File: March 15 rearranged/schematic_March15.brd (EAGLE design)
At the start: 200.3 x 216.6 mm, 315 parts, among them CON1 UBC05V128-B0C04D, IC1 FT232RL, IC10 TL084D, IC13 7805TV, IC3 TL084D, IC4 TL084D, IC5 TL084D, IC6 TL084D, IC7 TL084D, IC8 TL084D, IC9 TL084D, Q2 BC557, T1 BC547, T2 BC547, U1 TMS320F28069_PN_80, U10 REF2030AIDDCR, U2 TLV5610_PW_20, U3 REF2030AIDDCR, U4 REF2030AIDDCR, U5 TS12A44514DR, U6 TS12A44514DR, U7 TPS7333QD, U8 REF2030AIDDCR, U9 MAX395CWG+

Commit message: Rearranged analog part to make the board smaller
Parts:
- moved R66 22.8 mm to (110.4, 25.3), flipped to the bottom
- moved R67 22.7 mm to (110.3, 29.2), flipped to the bottom
- moved JP42 20.4 mm to (145.3, 17.2), turned to 270 degrees
- moved JP43 18.7 mm to (143.4, -12.3), turned to 90 degrees
- moved JP13 17.6 mm to (139.5, 17.1), turned to 270 degrees
- moved JP68 16.9 mm to (121.4, 35.6)
- moved JP16 16.8 mm to (137.5, -12.4), turned to 270 degrees
- moved R64 16.5 mm to (116.0, 20.8), flipped to the bottom, turned to 180 degrees
- moved D14 15.3 mm to (117.1, 16.5)
- moved R127 14.9 mm to (113.6, 16.7)
- moved D15 13.4 mm to (109.8, 16.5), turned to 90 degrees
- moved C66 12.1 mm to (115.7, 30.9), flipped to the bottom, turned to 0 degrees
- moved R49 11.3 mm to (109.0, 34.0)
- moved C27 11.3 mm to (104.1, 19.2)
- moved C75 11.3 mm to (102.9, 27.9)
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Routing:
- net +5V: track 1057.4 -> 964.1 mm, vias 18 -> 15
- net ADCINA5: track 93.9 -> 140.8 mm
- net INTINP6: track 34.9 -> 72.9 mm, vias 1 -> 3
- net -5V: track 665.3 -> 640.2 mm, vias 12 -> 11
- net INTSWITCH4: track 10.9 -> 35.1 mm, vias 1 -> 0
- net INTINP4: track 53.4 -> 74.8 mm, vias 0 -> 1
- net INT_CONTROL: track 134.8 -> 113.7 mm
- net +3V3: track 515.0 -> 494.5 mm, vias 20 -> 19
- net DACO7: track 109.2 -> 129.1 mm
- net DACO5: track 97.7 -> 114.2 mm, vias 2 -> 3
- net OUT3: track 8.50 -> 22.0 mm, vias 0 -> 1
- net X8: track 73.6 -> 86.8 mm
- net INTSWITCH8: track 66.8 -> 79.6 mm
- net X4: track 28.0 -> 39.8 mm
- net X6: track 31.8 -> 43.6 mm
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
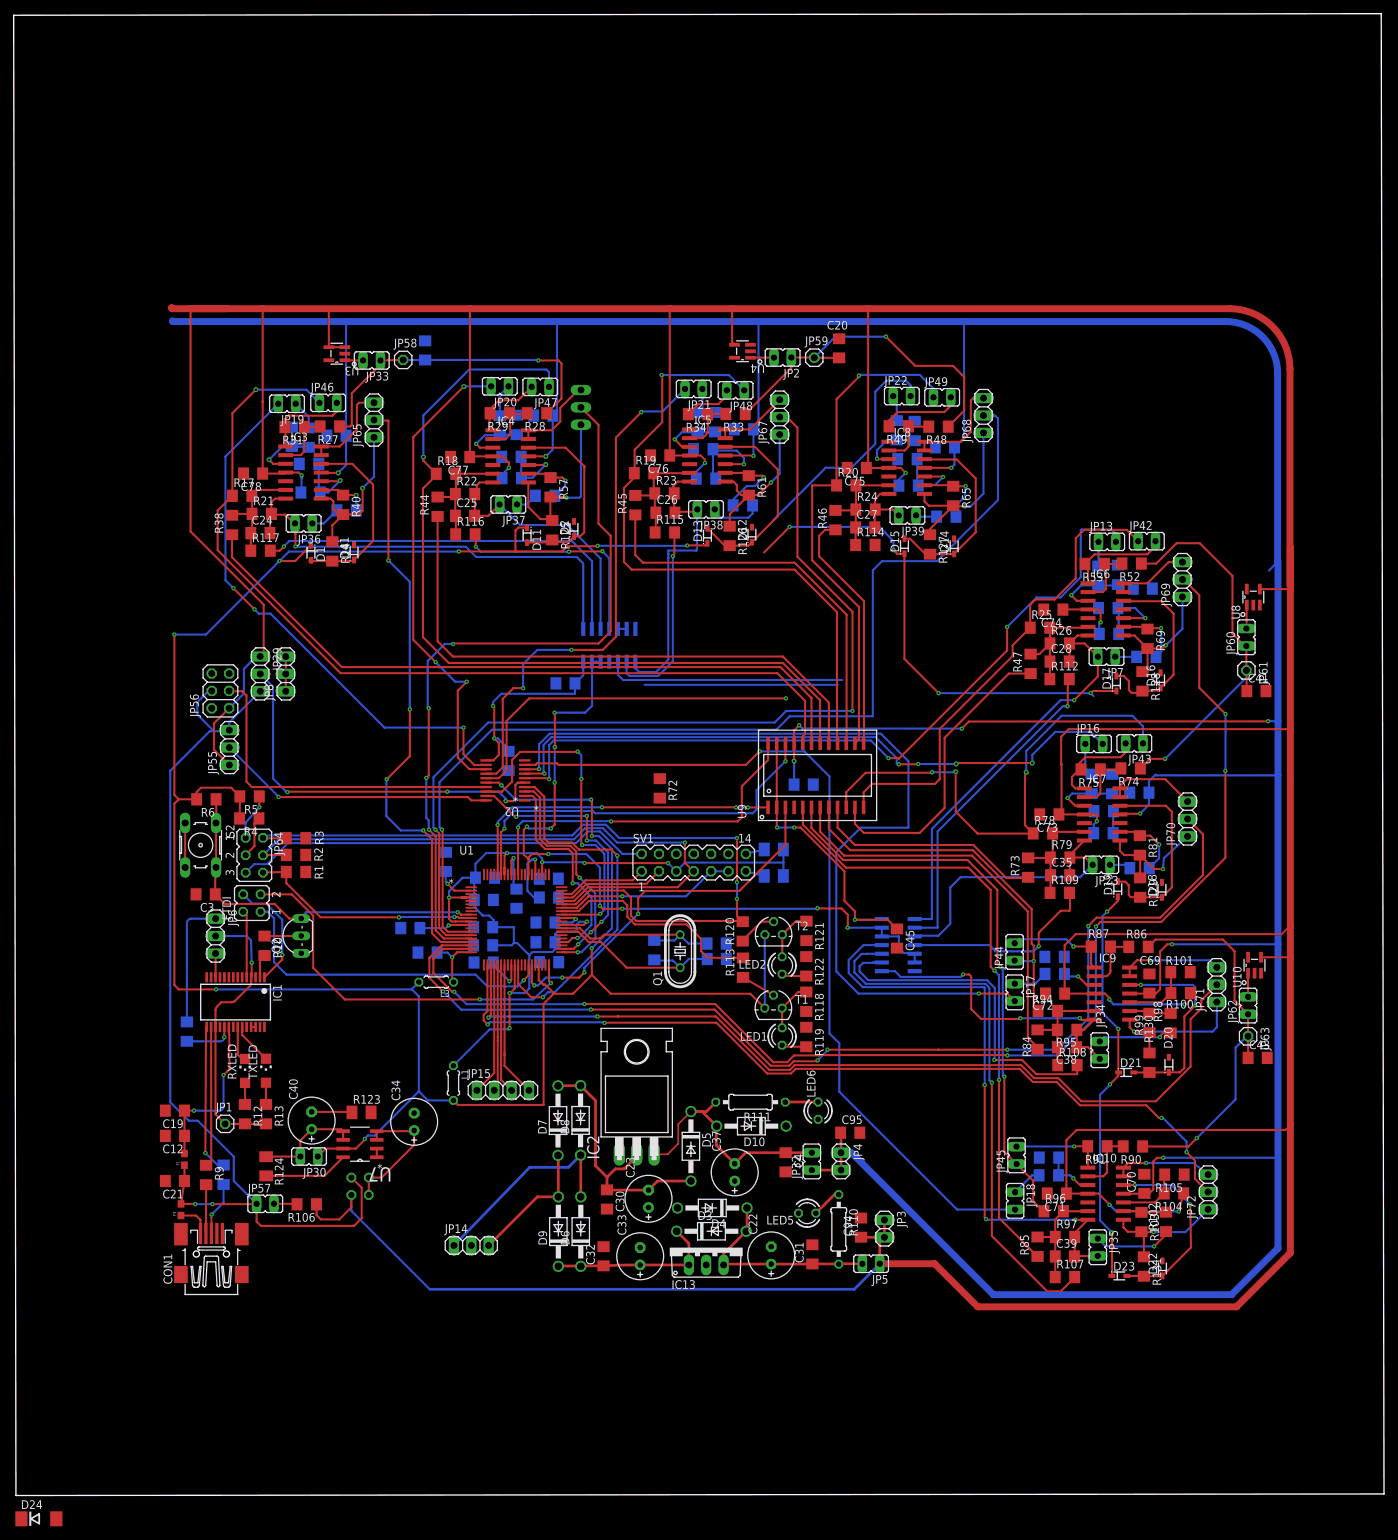
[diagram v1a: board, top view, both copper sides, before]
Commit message: Rearranged Stuff
Remaining - Ground Plane, Names, holes at the side, text (
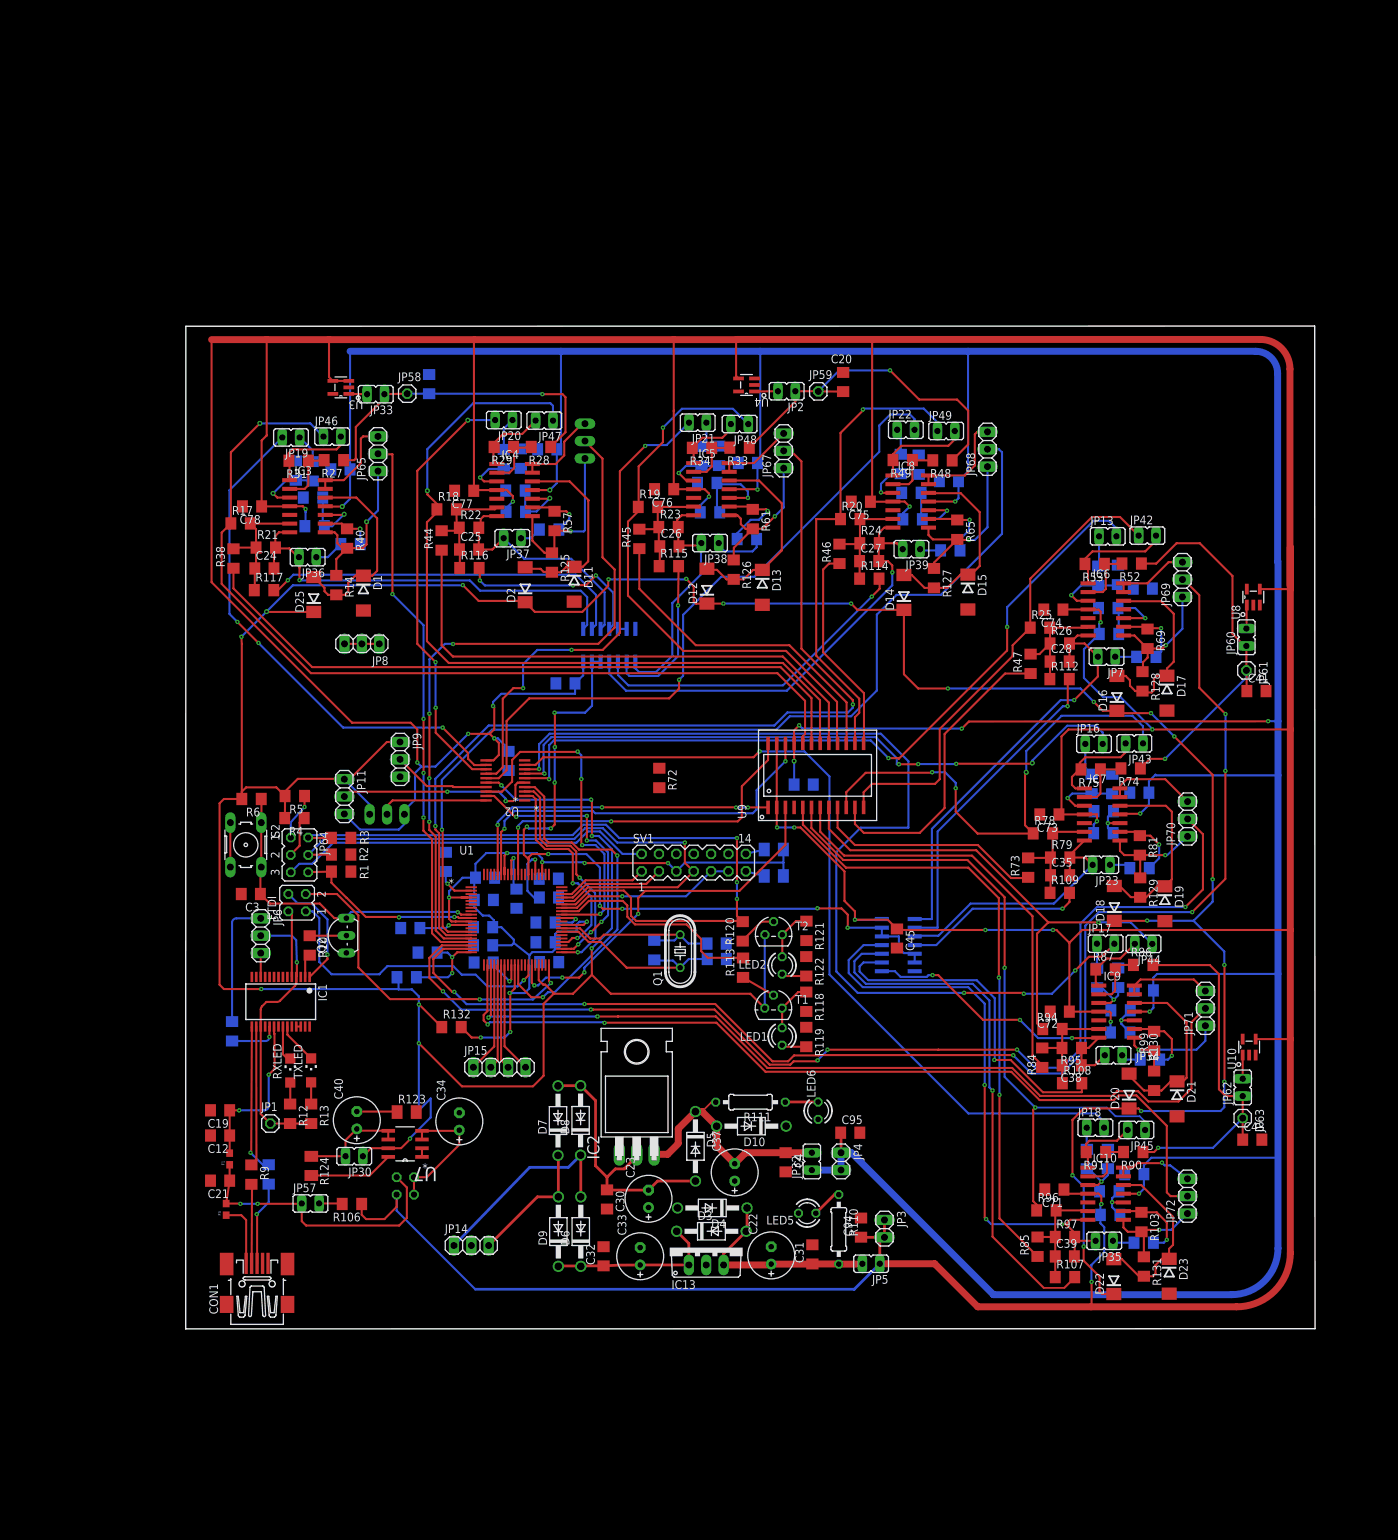
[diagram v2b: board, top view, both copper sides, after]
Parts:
- removed D24: (no value), diode:DO214AA
- removed D41: 1N914BWS, many_diodes:SOD323F
- removed JP29, JP55: (no value), pinhead:1X03
- removed JP56: (no value), pinhead:2X03
- removed L1, L3: BKP1005HS221-T, rcl:0204/5
- added D25: (no value), diode:DO214AA
- added JP10, JP11, JP9: (no value), pinhead:1X03
- added R132, R133: 0, resistor:R1206
- D1, D11, D12, D13, D14, D15, D16, D17, D18, D19, D2, D20, D21, D22, D23: value 1N914BWS -> (none); device many_diodes:SOD323F -> diode:DO214AA
- moved JP44 18.9 mm to (144.8, -41.7), turned to 90 degrees
- moved JP45 17.9 mm to (143.7, -68.9), turned to 90 degrees
- moved JP18 15.9 mm to (137.7, -68.5), turned to 270 degrees
- moved JP17 15.1 mm to (139.2, -41.6), turned to 270 degrees
- moved C43 12.0 mm to (160.7, -70.3)
- moved JP62 12.0 mm to (159.3, -62.6)
- moved JP63 12.0 mm to (159.3, -67.1)
- moved U10 12.0 mm to (160.2, -56.7)
- moved JP8 12.0 mm to (30.5, 2.21), turned to 180 degrees
- moved D15 11.4 mm to (119.1, 9.78), turned to 270 degrees
- moved D13 11.0 mm to (89.1, 10.5), turned to 270 degrees
- moved D2 10.8 mm to (54.4, 10.8)
- moved R100 10.6 mm to (141.4, -54.6), flipped to the bottom
- moved R101 10.4 mm to (141.4, -51.4), flipped to the bottom
- moved D12 9.99 mm to (80.9, 10.6)
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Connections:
- removed net N$131: JP55.2, U2.20
- removed net N$133: JP29.2, U2.5
- new net DVDD: JP10.2, U2.20
- new net PREBAR: JP11.2, U2.5
- net +3V3: now also D12.C, D14.C, D16.C, D18.C, D2.C, D20.C, D22.C, D25.C, JP10.3, JP11.1, JP9.1, R132.1, R133.1; no longer D1.C, D11.C, D13.C, D15.C, D17.C, D19.C, D21.C, D23.C, L1.2, L3.2
- net +5V: now also JP10.1, JP11.3; no longer JP29.1, JP55.1, JP56.1
- net ?????: now also JP9.2; no longer JP56.3
- net AGND: now also D1.A, D11.A, D13.A, D15.A, D17.A, D19.A, D21.A, D23.A; no longer D12.A, D14.A, D16.A, D18.A, D2.A, D20.A, D22.A, D41.A
- net BUFIN1: now also D1.C, D25.A; no longer D1.A, D41.C
- net BUFIN2: now also D11.C, D2.A; no longer D11.A, D2.C
- net BUFIN3: now also D12.A, D13.C; no longer D12.C, D13.A
- net BUFIN4: now also D14.A, D15.C; no longer D14.C, D15.A
- net BUFIN5: now also D16.A, D17.C; no longer D16.C, D17.A
- net BUFIN6: now also D18.A, D19.C; no longer D18.C, D19.A
- net BUFIN7: now also D20.A, D21.C; no longer D20.C, D21.A
- net BUFIN8: now also D22.A, D23.C; no longer D22.C, D23.A
- net GND: now also JP9.3; no longer JP56.5
- net N$7: now also R133.2; no longer L3.1
- net USB_VCC: no longer JP29.3, JP55.3, JP56.4
- net VDDIO: now also R132.2; no longer L1.1
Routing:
- net USB_VCC: track 138.0 -> 42.0 mm
- net +3V3: track 494.5 -> 583.0 mm, vias 19 -> 26
- net N$133: track 56.8 -> 0.00 mm, vias 3 -> 0
- net N$131: track 40.8 -> 0.00 mm, vias 1 -> 0
- net ?????: track 50.8 -> 14.2 mm
- net PREBAR: track 0.00 -> 29.7 mm, vias 0 -> 2
- net -5V: track 640.2 -> 610.7 mm
- net X4: track 39.8 -> 66.5 mm, vias 0 -> 1
- net +5V: track 964.1 -> 983.6 mm, vias 15 -> 19
- net INTINP7: track 55.8 -> 74.0 mm
- net INTINP8: track 83.8 -> 101.6 mm
- net DACO7: track 129.1 -> 146.4 mm, vias 2 -> 4
- net DVDD: track 0.00 -> 16.0 mm
- net INTSWITCH4: track 35.1 -> 48.2 mm, vias 0 -> 1
- net INTINP3: track 96.0 -> 84.3 mm
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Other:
- board size 200.3 x 216.6 mm -> 165.1 x 146.6 mm

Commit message: fixed schematic bugs
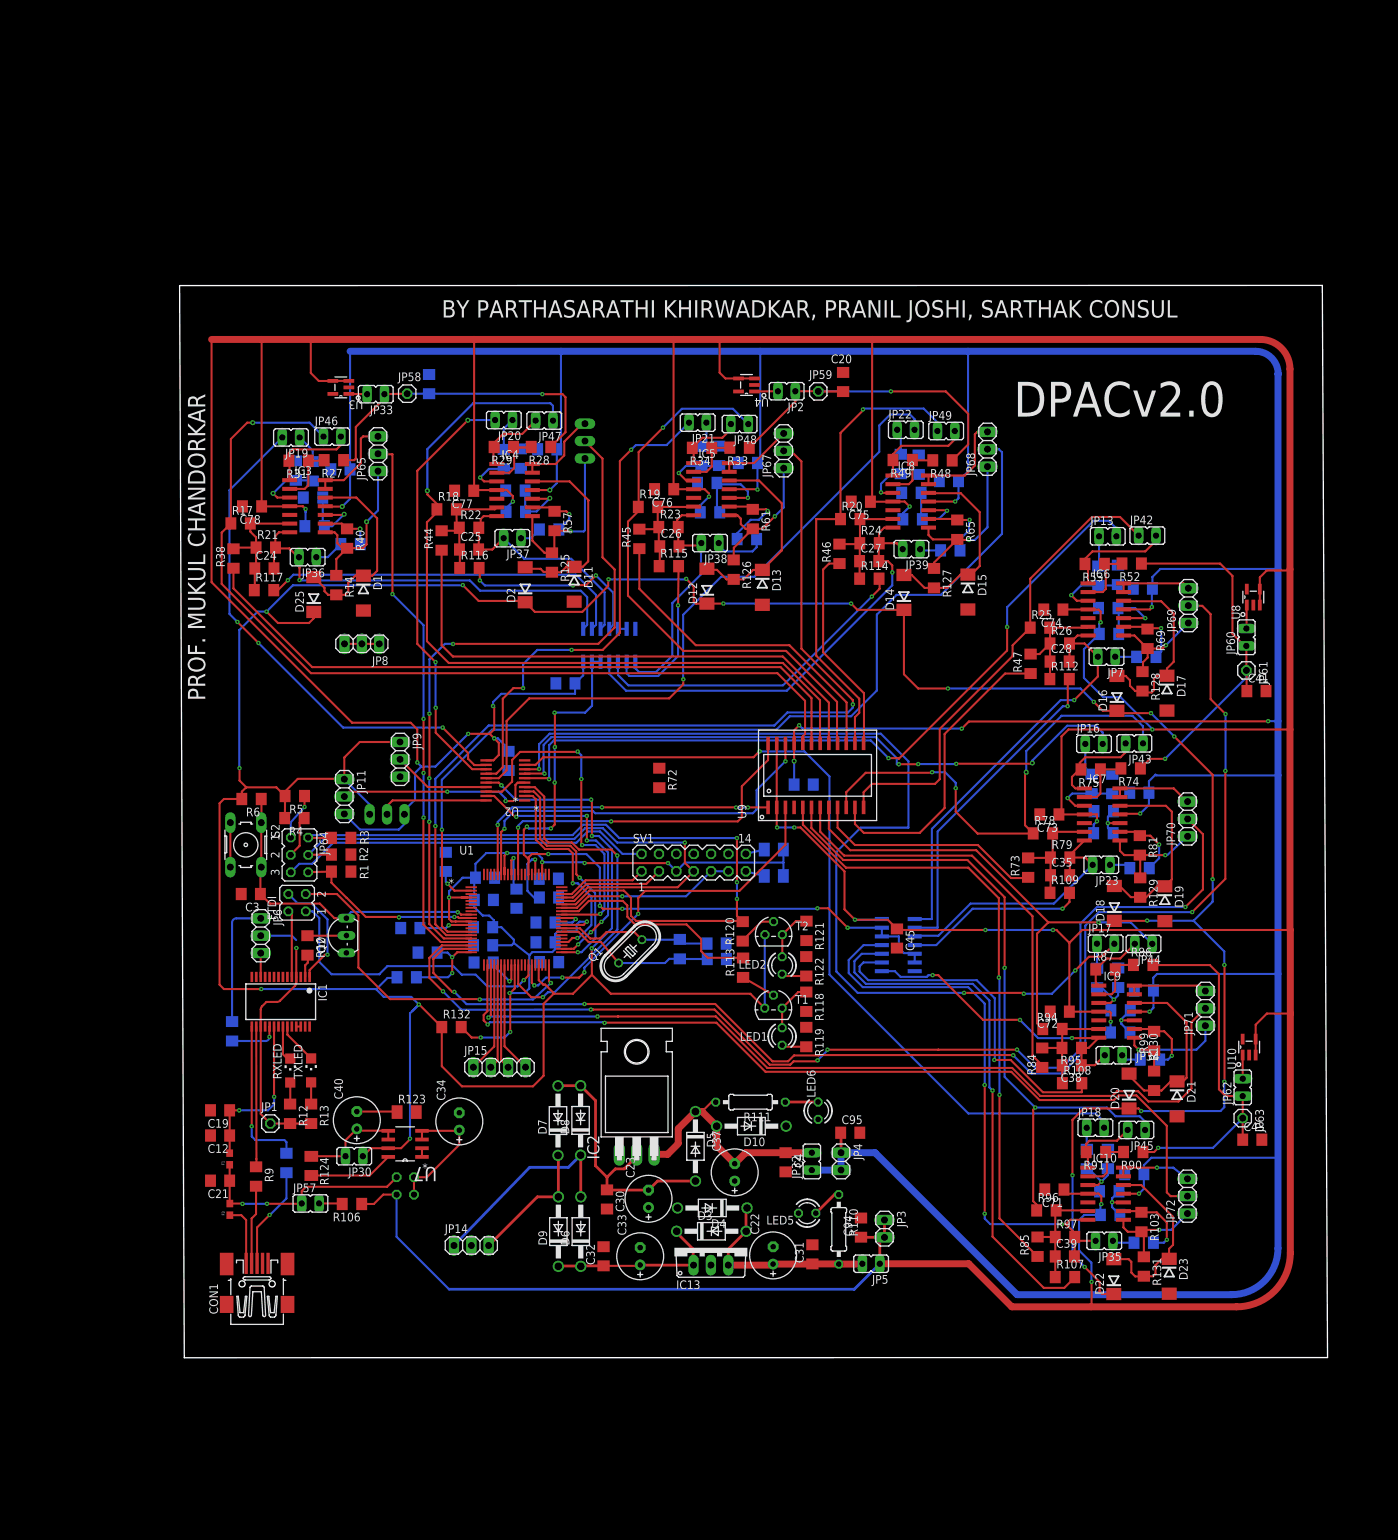
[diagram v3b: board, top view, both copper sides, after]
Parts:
- moved Q1 7.29 mm to (69.7, -42.7), turned to 45 degrees
- moved JP69 3.91 mm to (151.3, 7.80)
- moved R7 3.74 mm to (77.0, -42.4)
- moved R8 3.09 mm to (19.5, -73.7)
- moved R9 0.74 mm to (15.0, -75.7)
- moved IC13 0.69 mm to (81.5, -86.1)
- moved F3 0.53 mm to (11.2, -80.5)
- moved R10 0.33 mm to (22.6, -41.9)
- moved C22 0.28 mm to (90.6, -87.2)
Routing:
- net -5V: track 610.7 -> 638.3 mm, vias 11 -> 12
- net +5V: track 983.6 -> 995.9 mm
- net USB_VCC: track 42.0 -> 32.8 mm
- net X2CLK: track 28.2 -> 23.6 mm
- net X1CLK: track 26.8 -> 22.2 mm
- net OUT5: track 18.9 -> 15.5 mm
- net ADCINA0: track 199.8 -> 196.7 mm
- net +1.5V2: track 51.9 -> 49.1 mm
- net N$12: track 12.3 -> 15.1 mm
- net +3V3: track 583.0 -> 585.5 mm, vias 26 -> 25
- net +1.5V3: track 56.5 -> 54.1 mm
- net LIMO6: track 13.3 -> 12.0 mm
- net D+: track 21.9 -> 23.1 mm
- net INTINP1: track 134.6 -> 135.8 mm
- net 3V3_OUT: track 41.9 -> 40.7 mm
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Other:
- board size 165.1 x 146.6 mm -> 167.8 x 156.8 mm
- board text added: "BY PARTHASARATHI KHIRWADKAR, PRANIL JOSHI, SARTHAK CONSUL"
- board text added: "DPACv2.0"
- board text added: "PROF. MUKUL CHANDORKAR"
